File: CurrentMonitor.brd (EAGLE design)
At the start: 85 x 45 mm, 50 parts, among them J1 Ext Pwr, U1 NCP1117DT50G, U2 MCP1700, U3 ATmega328P-PU, Y1 16MHz 18pF

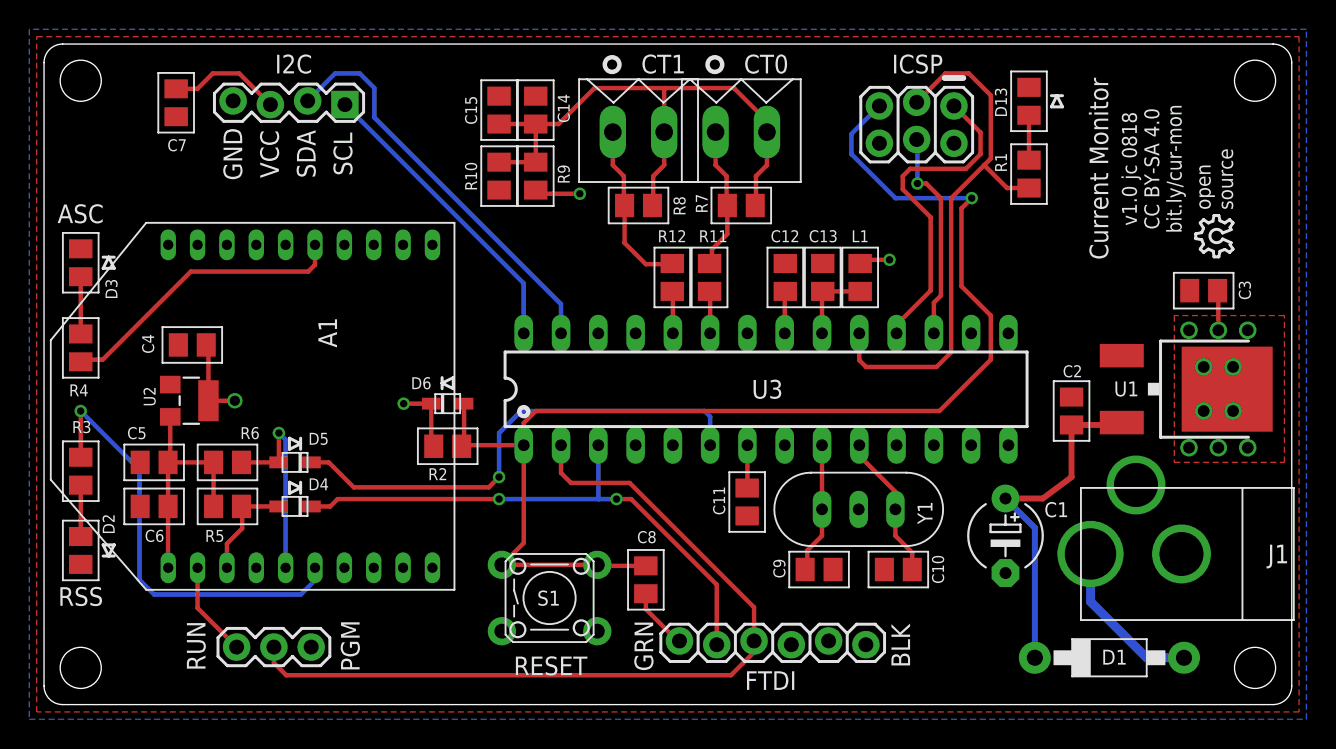
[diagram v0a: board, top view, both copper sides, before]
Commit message: Add terminal blocks for additional GPIO and LEDs.
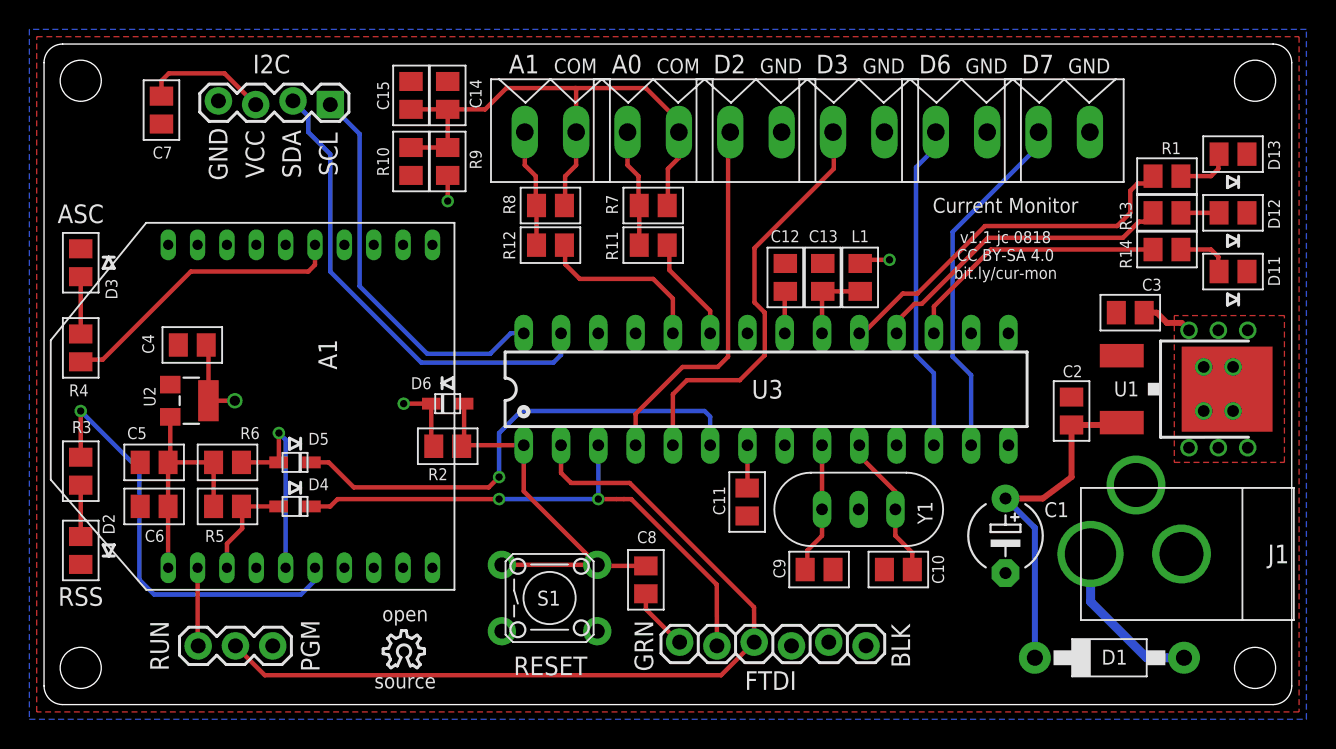
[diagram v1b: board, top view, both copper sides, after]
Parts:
- removed JP1: ICSP, _jc:2X3_LOCK
- added D11: Green, _jc:D0805
- added D12: Yellow, _jc:D0805
- added R13, R14: 1K, _jc:M0805
- added TB3: D2, _jc:OST-TB-2-3.5MM
- added TB4: D3, _jc:OST-TB-2-3.5MM
- added TB5: D6, _jc:OST-TB-2-3.5MM
- added TB6: D7, _jc:OST-TB-2-3.5MM
- D13: value HB -> Red
- TB1: value CT-0 -> A0
- TB2: value CT-1 -> A1
- moved LOGO1 64.3 mm to (23.1, 2.50), turned to 0 degrees
- moved D13 14.4 mm to (81.0, 37.5), turned to 0 degrees
- moved R1 9.40 mm to (76.5, 36.0), turned to 180 degrees
- moved R12 8.59 mm to (34.5, 31.3), turned to 180 degrees
- moved C14 6.08 mm to (25.0, 41.5)
- moved C15 6.08 mm to (27.5, 41.5)
- moved R10 6.08 mm to (25.0, 37.0)
- moved R9 6.08 mm to (27.5, 37.0)
- moved R7 6.00 mm to (41.5, 34.0)
- moved R8 6.00 mm to (34.5, 34.0)
- moved TB1 6.00 mm to (41.5, 39.0)
- moved TB2 6.00 mm to (34.5, 39.0)
- moved C3 5.22 mm to (74.0, 26.7)
- moved R11 4.43 mm to (41.5, 31.3), turned to 0 degrees
- moved JP4 2.62 mm to (10.5, 4.00)
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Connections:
- new net N$18: D11.A, R14.1
- new net N$9: D12.A, R13.1
- new net PD2: TB3.P$1, U3.4
- new net PD3: TB4.P$1, U3.5
- new net PD6: TB5.P$1, U3.12
- new net PD7: TB6.P$1, U3.13
- net /RESET: no longer JP1.5
- net GND: now also D11.K, D12.K, TB3.P$2, TB4.P$2, TB5.P$2, TB6.P$2; no longer JP1.6
- net MISO: now also R13.2; no longer JP1.1
- net MOSI: now also R14.2; no longer JP1.4
- net SCK: no longer JP1.3
- net VCC: no longer JP1.2
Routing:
- net /RESET: track 86.6 -> 27.3 mm, vias 1 -> 0
- net PD3: track 0.00 -> 28.6 mm
- net PD2: track 0.00 -> 25.4 mm
- net PD7: track 0.00 -> 24.3 mm
- net PD6: track 0.00 -> 22.4 mm
- net SCK: track 37.5 -> 25.3 mm
- net ADC1: track 2.88 -> 12.0 mm
- net SCL: track 20.6 -> 26.9 mm
- net SDA: track 27.7 -> 32.7 mm
- net ADC0: track 2.88 -> 7.22 mm
- net MOSI: track 14.4 -> 18.4 mm, vias 1 -> 0
- net N$18: track 0.00 -> 3.78 mm
- net N$16: track 11.8 -> 8.03 mm
- net N$9: track 0.00 -> 2.60 mm
- net N$15: track 9.78 -> 8.03 mm
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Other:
- board text added: "A0"
- board text added: "A1"
- board text added: "COM"
- board text added: "v1.1 jc 0818 CC BY-SA 4.0 bit.ly/cur-mon"
- board text removed: "CT0"
- board text removed: "CT1"
- board text removed: "ICSP"
- board text removed: "v1.0 jc 0818 CC BY-SA 4.0 bit.ly/cur-mon"

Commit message: Layout tweaks.
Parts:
- removed JP4: Run/Pgm, SparkFun:1X03
- added JP1: FTDI, SparkFun:1X06_LOCK
- C15: value 10uF -> 4.7uF
- JP2: value FTDI -> I2C; device SparkFun:1X06_LOCK -> SparkFun:1X04_LOCK
- JP3: value I2C -> Run/Pgm; device SparkFun:1X04_LOCK -> SparkFun:1X03
- R10, R9: value 2.2K -> 200
- R11, R12: value 1K -> 2.2K
- R2: value 10K -> 1K
- R4: value 1K -> 10K
- R5, R6: value 4.7K -> 1K
- R7, R8: value 200 -> 4.7K
- U2: value MCP1700 -> MCP1700T-3302E/TT
- moved R3 75.5 mm to (76.5, 31.0), turned to 180 degrees
- moved JP2 52.0 mm to (19.5, 41.0)
- moved R2 51.5 mm to (76.5, 33.5)
- moved LOGO2 44.5 mm to (35.5, 32.5), turned to 0 degrees
- moved R14 42.0 mm to (34.5, 31.3)
- moved JP3 38.1 mm to (10.5, 4.00), turned to 0 degrees
- moved R7 35.5 mm to (12.5, 13.5)
- moved R13 35.1 mm to (41.5, 31.3), turned to 0 degrees
- moved R8 28.1 mm to (12.5, 16.5), turned to 180 degrees
- moved R4 25.9 mm to (27.5, 17.6), turned to 180 degrees
- moved R11 15.1 mm to (27.5, 37.0), turned to 270 degrees
- moved R9 14.3 mm to (41.5, 34.0), turned to 180 degrees
- moved R6 12.7 mm to (2.50, 24.3), turned to 270 degrees
- moved R12 11.1 mm to (25.0, 37.0), turned to 90 degrees
- moved R5 10.3 mm to (2.50, 15.9), turned to 90 degrees
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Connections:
- net +3V3: now also R7.2, R8.2; no longer R5.2, R6.2
- net /RESET: now also R4.1; no longer R2.1
- net ADC0: now also R13.2; no longer R11.2
- net ADC1: now also R14.1; no longer R12.1
- net GND: now also JP1.1, JP1.2, JP2.4, R12.1; no longer JP2.1, JP2.2, JP3.4, R10.1
- net MISO: now also R2.2; no longer R13.2
- net MOSI: now also R3.2; no longer R14.2
- net N$10: now also JP3.1; no longer JP4.1
- net N$11: now also R5.1; no longer R3.1
- net N$12: now also R6.1; no longer R4.1
- net N$13: now also R5.2; no longer R3.2
- net N$14: now also R6.2; no longer R4.2
- net N$15: now also R13.1, R9.2; no longer R11.1, R7.2
- net N$16: now also R10.1, R14.2; no longer R12.2, R8.1
- net N$17: now also R8.1; no longer R6.1
- net N$18: now also R3.1; no longer R14.1
- net N$3: now also R11.1, R12.2; no longer R7.1, R8.2
- net N$8: now also R7.1; no longer R5.1
- net N$9: now also R2.1; no longer R13.1
- net RST: now also JP1.6; no longer JP2.6
- net RXD: now also JP1.4, JP3.2; no longer JP2.4, JP4.2
- net SCL: now also JP2.1; no longer JP3.1
- net SDA: now also JP2.2; no longer JP3.2
- net TXD: now also JP1.5; no longer JP2.5
- net VCC: now also JP1.3, R11.2, R4.2; no longer JP3.3, R2.2, R9.2
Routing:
- net N$13: track 29.9 -> 30.6 mm
- net SDA: track 32.7 -> 32.1 mm
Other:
- board text added: "INPUT 7-12 VDC"
- board text removed: "INPUT 7-12VDC"
